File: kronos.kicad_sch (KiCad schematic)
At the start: 0 parts

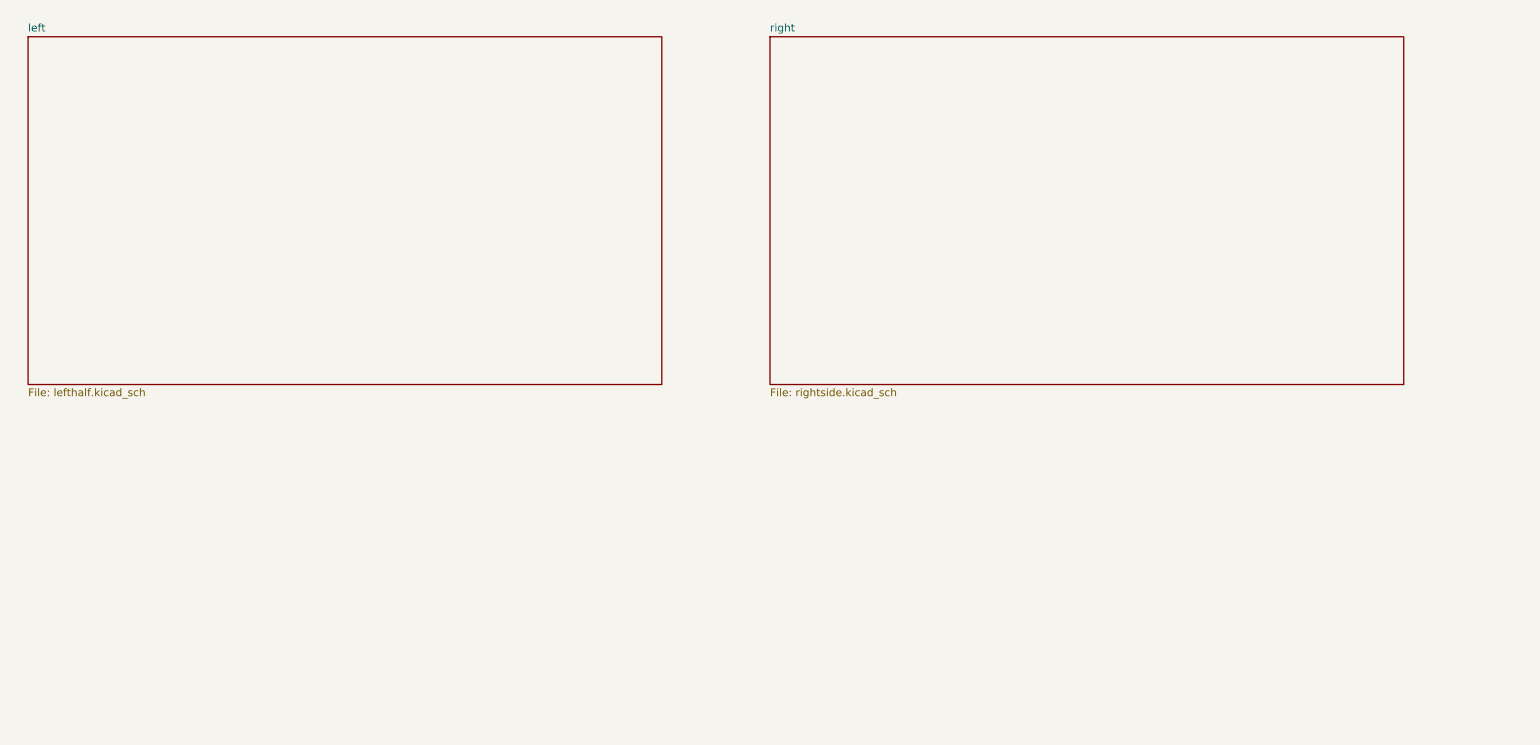
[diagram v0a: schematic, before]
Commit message: Rename schematic halves, update sheets and backups
Rename rightside.kicad_sch -> half.kicad_sch and lefthalf.kicad_sch -> side.kicad_sch; update sheet references, UUIDs, sheetfile names and sheet positions in kronos.kicad_sch and kronos.kicad_pro. Many symbol/text positions, junctions, wires and UUIDs were adjusted in the renamed/updated sheets to reflect the new layout. Clear used_designators in the project file. Rotate backup artifacts: remove two old kronos backups and add three new kronos-backups ZIPs; add ~kronos.kicad_pro.lck. This change reorganizes the schematic halves and updates project metadata and backups accordingly.
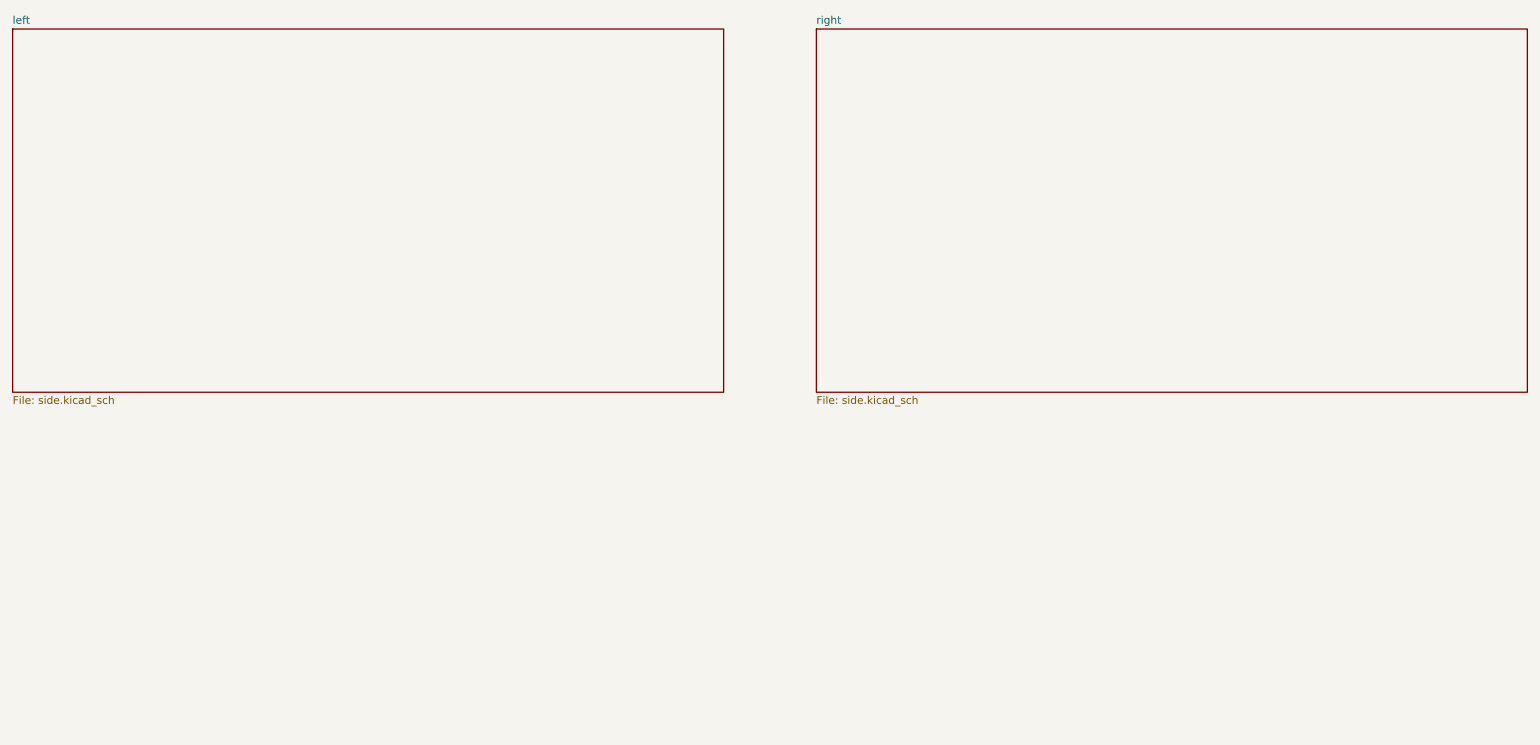
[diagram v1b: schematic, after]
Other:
- sheet left: file lefthalf.kicad_sch -> side.kicad_sch
- sheet right: file rightside.kicad_sch -> side.kicad_sch
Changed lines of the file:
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@@
 	(paper "A4")
 	(sheet
-		(at 151.13 59.69)
-		(size 104.14 57.15)
+		(at 26.67 58.42)
+		(size 116.84 59.69)
 		(exclude_from_sim no)
 		(in_bom yes)
@@
 			(color 0 0 0 0)
 		)
-		(property "Sheetname" "right"
-			(at 151.13 58.9784 0)
+		(property "Sheetname" "left"
+			(at 26.67 57.7084 0)
 			(show_name no)
 			(do_not_autoplace no)
@@
 			)
 		)
-		(property "Sheetfile" "rightside.kicad_sch"
-			(at 151.13 117.4246 0)
+		(property "Sheetfile" "side.kicad_sch"
+			(at 26.67 118.6946 0)
 			(show_name no)
 			(do_not_autoplace no)
@@
 	)
 	(sheet
-		(at 29.21 59.69)
-		(size 104.14 57.15)
+		(at 158.75 58.42)
+		(size 116.84 59.69)
 		(exclude_from_sim no)
 		(in_bom yes)
@@
 			(color 0 0 0 0)
 		)
-		(property "Sheetname" "left"
-			(at 29.21 58.9784 0)
+		(property "Sheetname" "right"
+			(at 158.75 57.7084 0)
 			(show_name no)
 			(do_not_autoplace no)
@@
 			)
 		)
-		(property "Sheetfile" "lefthalf.kicad_sch"
-			(at 29.21 117.4246 0)
+		(property "Sheetfile" "side.kicad_sch"
+			(at 158.75 118.6946 0)
 			(show_name no)
 			(do_not_autoplace no)

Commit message: PCB akmost done
PCB added; scheme update; blah blah
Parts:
- added BO1, BO2, BO3: Breakoff, symbol Mechanical:MountingHole
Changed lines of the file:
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@@
 	(generator_version "10.0")
 	(paper "A4")
+	(symbol
+		(lib_id "Mechanical:MountingHole")
+		(at 55.88 171.45 0)
+		(unit 1)
+		(body_style 1)
+		(exclude_from_sim no)
+		(in_bom no)
+		(on_board yes)
+		(in_pos_files yes)
+		(dnp no)
+		(fields_autoplaced yes)
+		(property "Reference" "BO1"
+			(at 58.42 170.1799 0)
+			(show_name no)
+			(do_not_autoplace no)
+			(effects
+				(font
+					(size 1.27 1.27)
+				)
+				(justify left)
+			)
+		)
+		(property "Value" "Breakoff"
+			(at 58.42 172.7199 0)
+			(show_name no)
+			(do_not_autoplace no)
+			(effects
+				(font
+					(size 1.27 1.27)
+				)
+				(justify left)
+			)
+		)
+		(property "Footprint" ""
+			(at 55.88 171.45 0)
+			(hide yes)
+			(show_name no)
+			(do_not_autoplace no)
+			(effects
+				(font
+					(size 1.27 1.27)
+				)
+			)
+		)
+		(property "Datasheet" ""
+			(at 55.88 171.45 0)
+			(hide yes)
+			(show_name no)
+			(do_not_autoplace no)
+			(effects
+				(font
+					(size 1.27 1.27)
+				)
+			)
+		)
+		(property "Description" "Mounting Hole without connection"
+			(at 55.88 171.45 0)
+			(hide yes)
+			(show_name no)
+			(do_not_autoplace no)
+			(effects
+				(font
+					(size 1.27 1.27)
+				)
+			)
+		)
+		(instances
+			(project "kronos"
+				(path "/05411d4e-5a66-4249-a10f-735e1ec24d10"
+					(reference "BO1")
+					(unit 1)
+				)
+			)
+		)
+	)
+	(symbol
+		(lib_id "Mechanical:MountingHole")
+		(at 93.98 171.45 0)
+		(unit 1)
+		(body_style 1)
+		(exclude_from_sim no)
+		(in_bom no)
+		(on_board yes)
+		(in_pos_files yes)
+		(dnp no)
+		(fields_autoplaced yes)
+		(property "Reference" "BO3"
+			(at 96.52 170.1799 0)
+			(show_name no)
+			(do_not_autoplace no)
+			(effects
+				(font
+					(size 1.27 1.27)
+				)
+				(justify left)
+			)
+		)
+		(property "Value" "Breakoff"
+			(at 96.52 172.7199 0)
+			(show_name no)
+			(do_not_autoplace no)
+			(effects
+				(font
+					(size 1.27 1.27)
+				)
+				(justify left)
+			)
+		)
+		(property "Footprint" ""
+			(at 93.98 171.45 0)
+			(hide yes)
+			(show_name no)
+			(do_not_autoplace no)
+			(effects
+				(font
+					(size 1.27 1.27)
+				)
+			)
+		)
+		(property "Datasheet" ""
+			(at 93.98 171.45 0)
+			(hide yes)
+			(show_name no)
+			(do_not_autoplace no)
+			(effects
+				(font
+					(size 1.27 1.27)
+				)
+			)
+		)
+		(property "Description" "Mounting Hole without connection"
+			(at 93.98 171.45 0)
+			(hide yes)
+			(show_name no)
+			(do_not_autoplace no)
+			(effects
+				(font
+					(size 1.27 1.27)
+				)
+			)
+		)
+		(instances
+			(project "kronos"
+				(path "/05411d4e-5a66-4249-a10f-735e1ec24d10"
+					(reference "BO3")
+					(unit 1)
+				)
+			)
+		)
+	)
+	(symbol
+		(lib_id "Mechanical:MountingHole")
+		(at 76.2 171.45 0)
+		(unit 1)
+		(body_style 1)
+		(exclude_from_sim no)
+		(in_bom no)
+		(on_board yes)
+		(in_pos_files yes)
+		(dnp no)
+		(property "Reference" "BO2"
+			(at 78.74 170.1799 0)
+			(show_name no)
+			(do_not_autoplace no)
+			(effects
+				(font
+					(size 1.27 1.27)
+				)
+				(justify left)
+			)
+		)
+		(property "Value" "Breakoff"
+			(at 78.994 172.466 0)
+			(show_name no)
+			(do_not_autoplace no)
+			(effects
+				(font
+					(size 1.27 1.27)
+				)
+				(justify left)
+			)
+		)
+		(property "Footprint" ""
+			(at 76.2 171.45 0)
+			(hide yes)
+			(show_name no)
+			(do_not_autoplace no)
+			(effects
+				(font
+					(size 1.27 1.27)
+				)
+			)
+		)
+		(property "Datasheet" ""
+			(at 76.2 171.45 0)
+			(hide yes)
+			(show_name no)
+			(do_not_autoplace no)
+			(effects
+				(font
+					(size 1.27 1.27)
+				)
+			)
+		)
+		(property "Description" "Mounting Hole without connection"
+			(at 76.2 171.45 0)
+			(hide yes)
+			(show_name no)
+			(do_not_autoplace no)
+			(effects
+				(font
+					(size 1.27 1.27)
+				)
+			)
+		)
+		(instances
+			(project "kronos"
+				(path "/05411d4e-5a66-4249-a10f-735e1ec24d10"
+					(reference "BO2")
+					(unit 1)
+				)
+			)
+		)
+	)
 	(sheet
 		(at 26.67 58.42)
